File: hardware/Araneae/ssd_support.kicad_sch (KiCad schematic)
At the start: 19 parts, among them U13 TPS22946YZPR, U14 NC7SB3157P6X, U15 NC7SB3157P6X

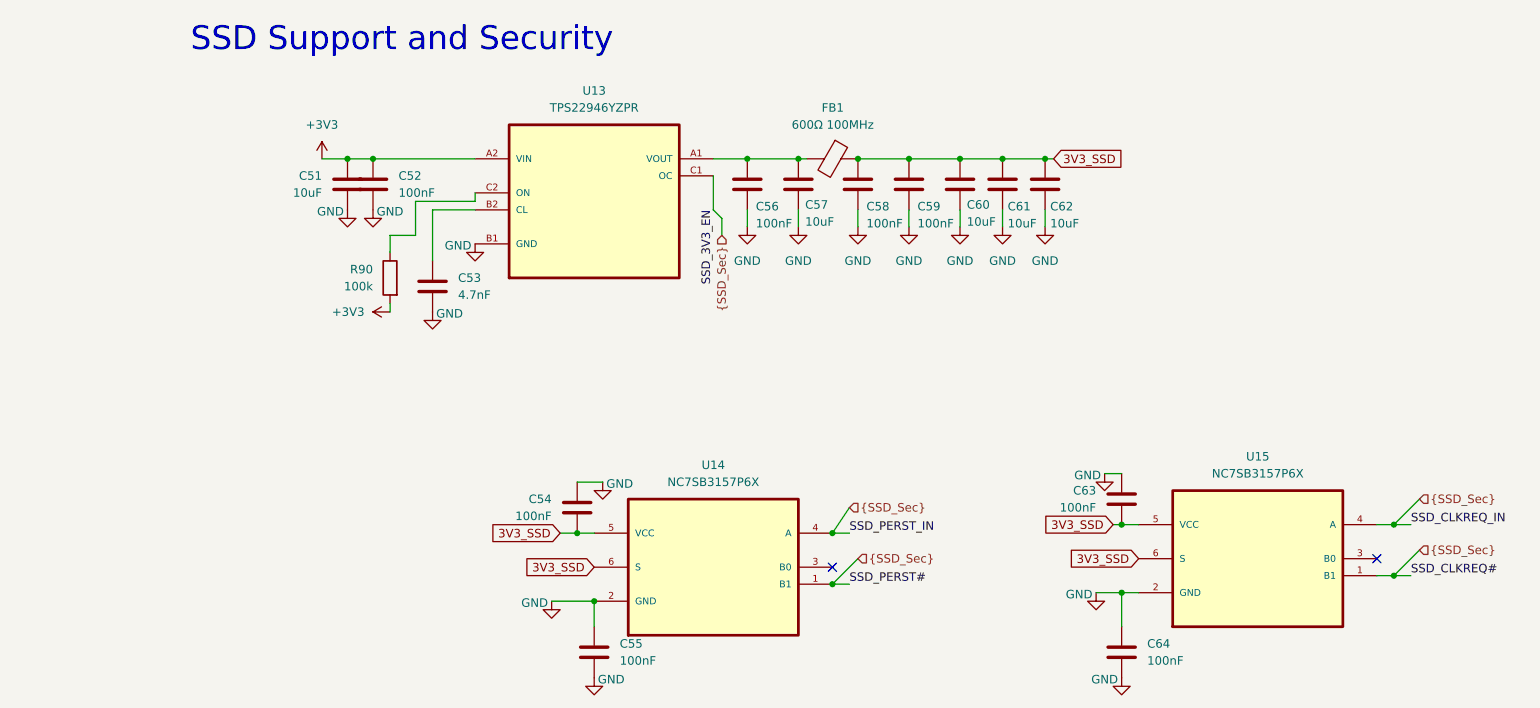
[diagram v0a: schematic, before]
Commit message: Add CI workflow for PCB checks and artifact generation
- Created a GitHub Actions workflow (`ci.yml`) to automate hardware checks including ERC, DRC, and plot generation for KiCad projects.
- Added a new footprint for the SON50P200X200X80-9N component in `SON50P200X200X80-9N.kicad_mod`.
- Introduced a new symbol for the TPS22965DSGR component in `TPS22965DSGR.kicad_sym`.
- Added a configuration file `kibot.yaml` for generating fabrication files and other outputs.
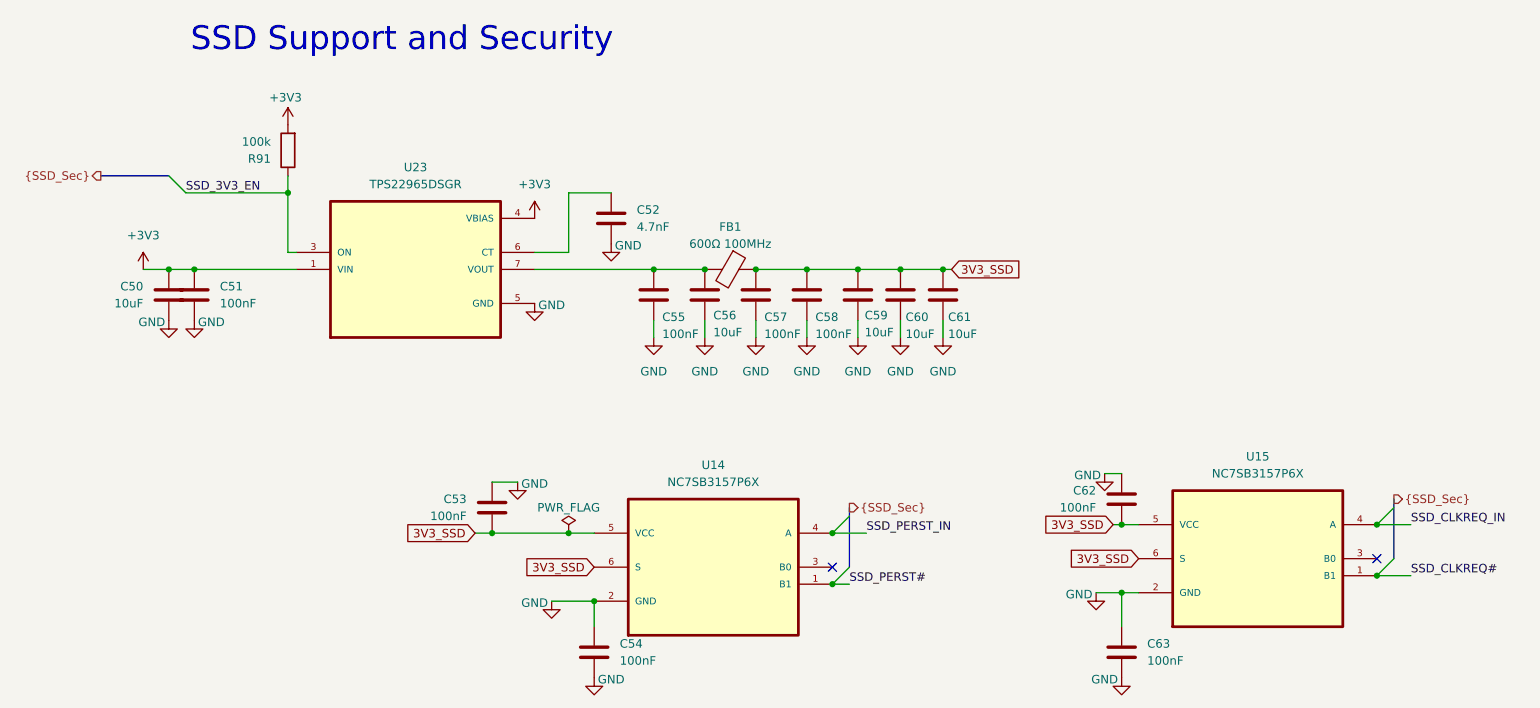
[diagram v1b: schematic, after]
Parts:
- removed C53: 4.7nF, symbol Device:C
- removed C62: 10uF, symbol Device:C
- removed R90: 100k, symbol Device:R
- removed U13: TPS22946YZPR, TPS22946YZPR:BGA6C50P2X3_140X90X50, symbol TPS22946YZPR:TPS22946YZPR
- added C50: 10uF, Capacitor_SMD:C_0603_1608Metric, symbol Device:C
- added C55: 100nF, Capacitor_SMD:C_0603_1608Metric, symbol Device:C
- added R91: 100k, Resistor_SMD:R_0603_1608Metric, symbol Device:R
- added U23: TPS22965DSGR, OPL:SON50P200X200X80-9N, symbol TPS22965DSGR:TPS22965DSGR
- C51, C57: value 10uF -> 100nF; footprint (none) -> Capacitor_SMD:C_0805_2012Metric
- C52: value 100nF -> 4.7nF; footprint (none) -> Capacitor_SMD:C_0603_1608Metric
- C53: renamed from C54; footprint (none) -> Capacitor_SMD:C_0603_1608Metric
- C54: renamed from C55; footprint (none) -> Capacitor_SMD:C_0603_1608Metric
- C56, C59: value 100nF -> 10uF; footprint (none) -> Capacitor_SMD:C_0603_1608Metric
- C58: footprint (none) -> Capacitor_SMD:C_0603_1608Metric
- C60, C61: footprint (none) -> Capacitor_SMD:C_0805_2012Metric
- C62: renamed from C63; footprint (none) -> Capacitor_SMD:C_0805_2012Metric
- C63: renamed from C64; footprint (none) -> Capacitor_SMD:C_0603_1608Metric
- FB1: footprint (none) -> Inductor_SMD:L_0805_2012Metric
- U14, U15: footprint NC7SB3157P6X:SOT65P210X110-6N -> OPL:SOT65P210X110-6N
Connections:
- net +3V3: now also C50.1, R91.2, U23.1 (VIN), U23.2 (VIN), U23.4 (VBIAS); no longer C52.1
- net 3V3_SSD: now also C57.1
- net GND: now also C50.2, C55.2, U23.5 (GND), U23.9 (GND), U23.9_1 (GND), U23.9_2 (GND)
- net {SSD_Sec}: no longer U14.1 (B1), U14.4 (A), U15.1 (B1), U15.4 (A)
- net at C56.1, FB1.2: now also C55.1, U23.7 (VOUT), U23.8 (VOUT); no longer C57.1
- new net: C52.1, U23.6 (CT)
- new net SSD_3V3_EN: R91.1, U23.3 (ON)
- new net SSD_CLKREQ#: U15.1 (B1)
- new net SSD_CLKREQ_IN: U15.4 (A)
- new net SSD_PERST#: U14.1 (B1)
- new net SSD_PERST_IN: U14.4 (A)
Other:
- company: (none) -> Matheus Henrique(Aka: TheusHen)
- title: (none) -> Araneae
- moved on the sheet: C53
